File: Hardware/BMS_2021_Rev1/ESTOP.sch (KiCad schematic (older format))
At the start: 11 parts

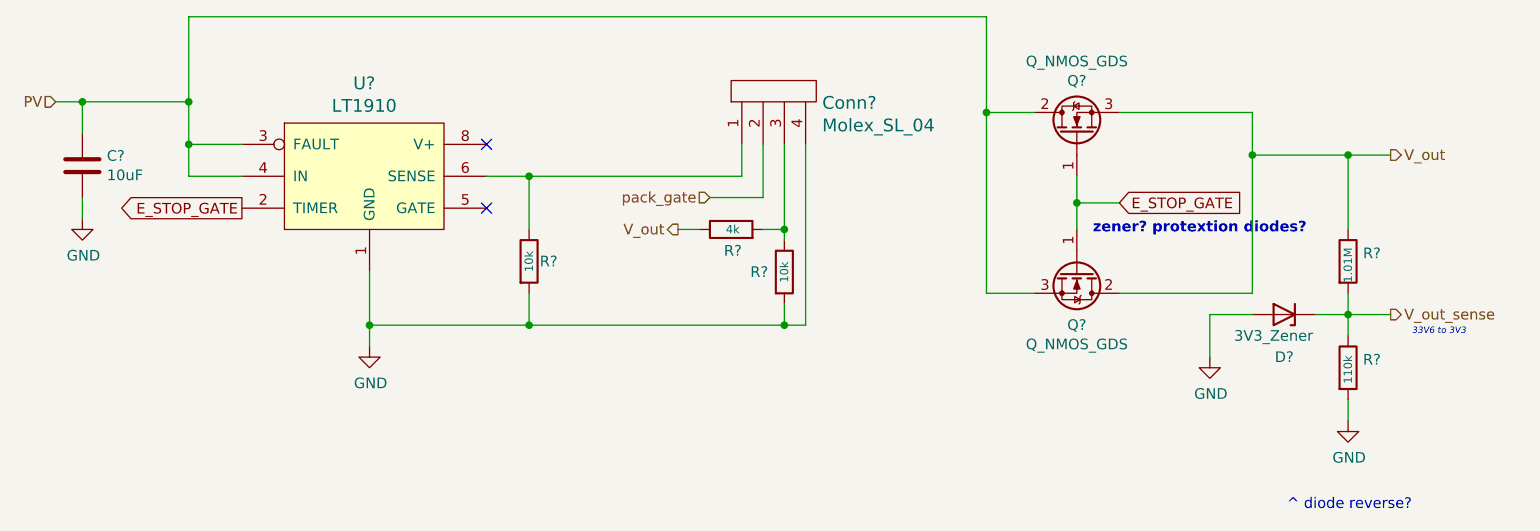
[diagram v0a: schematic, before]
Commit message: added libraries to docs folder
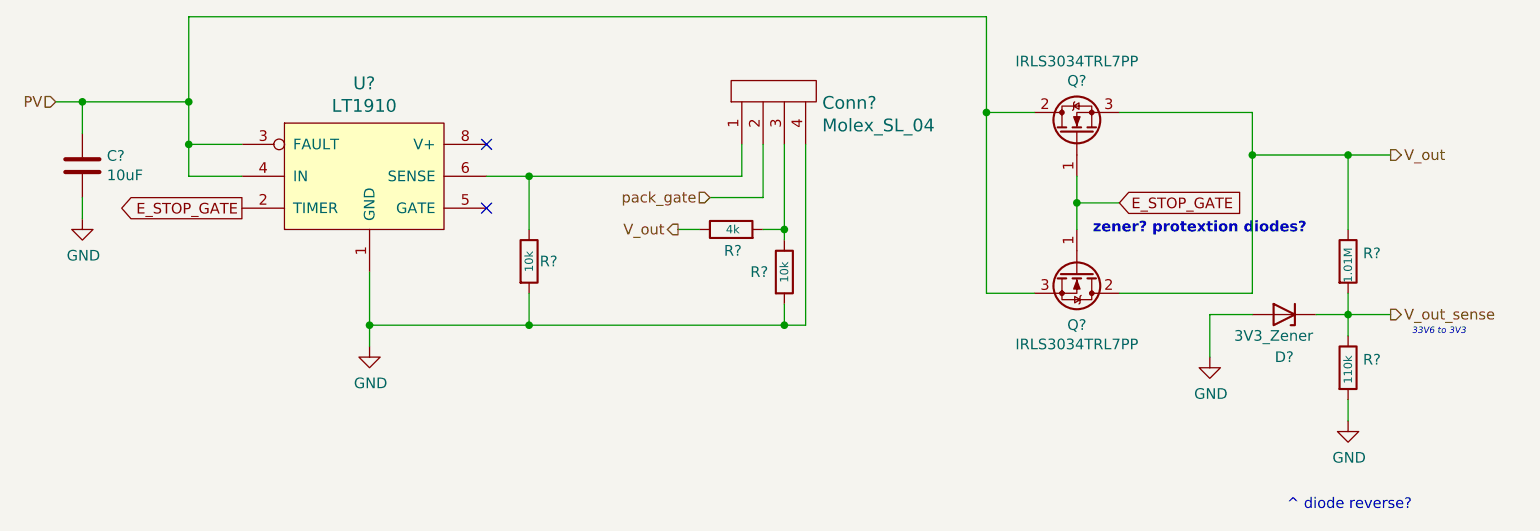
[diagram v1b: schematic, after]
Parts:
- Q? (x2): value Q_NMOS_GDS -> IRLS3034TRL7PP
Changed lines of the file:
@@
 P 7275 3300
 F 0 "Q?" V 7524 3300 50  0000 C CNN
-F 1 "Q_NMOS_GDS" V 7615 3300 50  0000 C CNN
+F 1 "IRLS3034TRL7PP" V 7615 3300 50  0000 C CNN
 F 2 "" H 7475 3400 50  0001 C CNN
-F 3 "~" H 7275 3300 50  0001 C CNN
+F 3 "https://www.digikey.com/en/products/detail/infineon-technologies/IRLS3034TRL7PP/2096641" H 7275 3300 50  0001 C CNN
 	1    7275 3300
 	0    1    1    0
@@
 P 7275 2650
 F 0 "Q?" V 7524 2650 50  0000 C CNN
-F 1 "Q_NMOS_GDS" V 7615 2650 50  0000 C CNN
+F 1 "IRLS3034TRL7PP" V 7615 2650 50  0000 C CNN
 F 2 "" H 7475 2750 50  0001 C CNN
-F 3 "~" H 7275 2650 50  0001 C CNN
+F 3 "https://www.digikey.com/en/products/detail/infineon-technologies/IRLS3034TRL7PP/2096641" H 7275 2650 50  0001 C CNN
 	1    7275 2650
 	0    -1   -1   0

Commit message: annotated sch.
some ICs got moved around- solve later
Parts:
- added D17: 3V3_Zener, symbol Device:D_Zener
- C11: renamed from C?; value 10uF -> 10u
- Q2, Q3: renamed from Q?; value IRLS3034TRL7PP -> IRLB3034PBF
- gave numbers to parts that had none: 8
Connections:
- net E_STOP_GATE: now also D17.1 (K)
- net GND: now also D17.2 (A)
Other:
- note removed: "^ diode reverse?"
- note removed: "zener? protextion diodes?"
- moved on the sheet: R40, R41
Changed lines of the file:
@@
 $EndDescr
 $Comp
-L MRDT_ICs:LT1910 U?
+L MRDT_ICs:LT1910 U7
 U 1 1 5F8B7AE9
 P 3550 3100
-F 0 "U?" H 3925 3787 60  0000 C CNN
+F 0 "U7" H 3925 3787 60  0000 C CNN
 F 1 "LT1910" H 3925 3681 60  0000 C CNN
 F 2 "" H 3550 3100 60  0001 C CNN
@@
 Connection ~ 3100 2700
 $Comp
-L Device:C C?
+L Device:C C11
 U 1 1 5F8B88FB
 P 2600 2800
-F 0 "C?" H 2715 2846 50  0000 L CNN
-F 1 "10uF" H 2715 2755 50  0000 L CNN
+F 0 "C11" H 2715 2846 50  0000 L CNN
+F 1 "10u" H 2715 2755 50  0000 L CNN
 F 2 "" H 2638 2650 50  0001 C CNN
 F 3 "~" H 2600 2800 50  0001 C CNN
@@
 	2600 2950 2600 3050
 $Comp
-L power:GND #PWR?
+L power:GND #PWR045
 U 1 1 5F8B8E29
 P 2600 3050
-F 0 "#PWR?" H 2600 2800 50  0001 C CNN
+F 0 "#PWR045" H 2600 2800 50  0001 C CNN
 F 1 "GND" H 2605 2877 50  0000 C CNN
 F 2 "" H 2600 3050 50  0001 C CNN
@@
 Connection ~ 4700 3550
 $Comp
-L Device:R R?
+L Device:R R37
 U 1 1 5F8B9A73
 P 4700 3250
-F 0 "R?" H 4750 3250 50  0000 L CNN
+F 0 "R37" H 4750 3250 50  0000 L CNN
 F 1 "10k" V 4700 3200 39  0000 L CNN
 F 2 "" V 4630 3250 50  0001 C CNN
@@
 	4700 3400 4700 3550
 $Comp
-L MRDT_Connectors:Molex_SL_04 Conn?
+L MRDT_Connectors:Molex_SL_04 Conn5
 U 1 1 5F8BA191
 P 6050 2500
-F 0 "Conn?" V 6045 2472 60  0000 R CNN
-F 1 "Molex_SL_04" V 5939 2472 60  0000 R CNN
+F 0 "Conn5" V 6100 3200 60  0000 R CNN
+F 1 "Molex_SL_04" V 6000 3475 60  0000 R CNN
 F 2 "" H 6050 2500 60  0001 C CNN
 F 3 "" H 6050 2500 60  0001 C CNN
@@
 	6000 3550 6000 2700
 $Comp
-L Device:R R?
+L Device:R R39
 U 1 1 5F8BD200
 P 5900 3300
-F 0 "R?" H 5740 3300 50  0000 L CNN
+F 0 "R39" H 5700 3300 50  0000 L CNN
 F 1 "10k" V 5900 3250 39  0000 L CNN
 F 2 "" V 5830 3300 50  0001 C CNN
@@
 	5800 2950 5550 2950
 $Comp
-L Device:R R?
+L Device:R R38
 U 1 1 5F8BD8B6
 P 5650 3100
-F 0 "R?" V 5550 3050 50  0000 L CNN
+F 0 "R38" V 5550 3050 50  0000 L CNN
 F 1 "4k" V 5650 3060 39  0000 L CNN
 F 2 "" V 5580 3100 50  0001 C CNN
@@
 Connection ~ 3950 3550
 $Comp
-L power:GND #PWR?
+L power:GND #PWR046
 U 1 1 5F8C9892
 P 3950 3650
-F 0 "#PWR?" H 3950 3400 50  0001 C CNN
+F 0 "#PWR046" H 3950 3400 50  0001 C CNN
 F 1 "GND" H 3955 3477 50  0000 C CNN
 F 2 "" H 3950 3650 50  0001 C CNN
@@
 $EndComp
 $Comp
-L Device:Q_NMOS_GDS Q?
+L Device:Q_NMOS_GDS Q3
 U 1 1 5F8F3525
 P 7275 3300
-F 0 "Q?" V 7524 3300 50  0000 C CNN
-F 1 "IRLS3034TRL7PP" V 7615 3300 50  0000 C CNN
+F 0 "Q3" V 7524 3300 50  0000 C CNN
+F 1 "IRLB3034PBF" V 7615 3300 50  0000 C CNN
 F 2 "" H 7475 3400 50  0001 C CNN
-F 3 "https://www.digikey.com/en/products/detail/infineon-technologies/IRLS3034TRL7PP/2096641" H 7275 3300 50  0001 C CNN
+F 3 "https://www.digikey.com/en/products/detail/infineon-technologies/IRLB3034PBF/2096638" H 7275 3300 50  0001 C CNN
 	1    7275 3300
 	0    1    1    0
 $EndComp
 $Comp
-L Device:Q_NMOS_GDS Q?
+L Device:Q_NMOS_GDS Q2
 U 1 1 5F8F352B
 P 7275 2650
-F 0 "Q?" V 7524 2650 50  0000 C CNN
-F 1 "IRLS3034TRL7PP" V 7615 2650 50  0000 C CNN
+F 0 "Q2" V 7524 2650 50  0000 C CNN
+F 1 "IRLB3034PBF" V 7615 2650 50  0000 C CNN
 F 2 "" H 7475 2750 50  0001 C CNN
-F 3 "https://www.digikey.com/en/products/detail/infineon-technologies/IRLS3034TRL7PP/2096641" H 7275 2650 50  0001 C CNN
+F 3 "https://www.digikey.com/en/products/detail/infineon-technologies/IRLB3034PBF/2096638" H 7275 2650 50  0001 C CNN
 	1    7275 2650
 	0    -1   -1   0
@@
 	7275 2975 7275 3100
 Wire Wire Line
-	7075 2550 6850 2550
-Wire Wire Line
-	6850 3400 7075 3400
-Wire Wire Line
 	7475 2550 8100 2550
 Wire Wire Line
@@
 Wire Wire Line
 	8100 3400 7475 3400
-Wire Wire Line
-	8100 2750 8550 2750
 Connection ~ 8100 2750
 Wire Wire Line
 	8100 2750 8100 3400
-Connection ~ 8550 2750
-Wire Wire Line
-	8550 2750 8750 2750
 Text HLabel 8750 2750 2    50   Output ~ 0
 V_out
@@
 L Device:R R?
 U 1 1 5F8F354D
-P 8550 3250
+P 8575 3250
 AR Path="/5F80136E/5F8F354D" Ref="R?"  Part="1"
 AR Path="/5F8CBCAE/5F8F354D" Ref="R?"  Part="1"
-AR Path="/5F801232/5F8F354D" Ref="R?"  Part="1"
-F 0 "R?" H 8620 3288 50  0000 L CNN
-F 1 "1.01M" V 8550 3150 39  0000 L CNN
-F 2 "" V 8480 3250 50  0001 C CNN
-F 3 "~" H 8550 3250 50  0001 C CNN
-	1    8550 3250
-	1    0    0    -1
-$EndComp
-$Comp
-L Device:R R?
+AR Path="/5F801232/5F8F354D" Ref="R40"  Part="1"
+F 0 "R40" H 8645 3288 50  0000 L CNN
+F 1 "1.01M" V 8575 3150 39  0000 L CNN
+F 2 "" V 8505 3250 50  0001 C CNN
+F 3 "~" H 8575 3250 50  0001 C CNN
+	1    8575 3250
+	1    0    0    -1
+$EndComp
+$Comp
+L Device:R R41
 U 1 1 5F8F3553
-P 8550 3750
-F 0 "R?" H 8620 3788 50  0000 L CNN
-F 1 "110k" V 8550 3675 39  0000 L CNN
-F 2 "" V 8480 3750 50  0001 C CNN
-F 3 "~" H 8550 3750 50  0001 C CNN
-	1    8550 3750
-	1    0    0    -1
-$EndComp
-Wire Wire Line
-	8550 3900 8550 4000
-Wire Wire Line
-	8550 3500 8750 3500
-Connection ~ 8550 3500
-Wire Wire Line
-	8550 3500 8550 3600
-$Comp
-L power:GND #PWR?
+P 8575 3750
+F 0 "R41" H 8645 3788 50  0000 L CNN
+F 1 "110k" V 8575 3675 39  0000 L CNN
+F 2 "" V 8505 3750 50  0001 C CNN
+F 3 "~" H 8575 3750 50  0001 C CNN
+	1    8575 3750
+	1    0    0    -1
+$EndComp
+Wire Wire Line
+	8575 3900 8575 4000
+Wire Wire Line
+	8575 3500 8775 3500
+Connection ~ 8575 3500
+Wire Wire Line
+	8575 3500 8575 3600
+$Comp
+L power:GND #PWR049
 U 1 1 5F8F355D
-P 8550 4000
-F 0 "#PWR?" H 8550 3750 50  0001 C CNN
-F 1 "GND" H 8555 3827 50  0000 C CNN
-F 2 "" H 8550 4000 50  0001 C CNN
-F 3 "" H 8550 4000 50  0001 C CNN
-	1    8550 4000
-	1    0    0    -1
-$EndComp
-$Comp
-L Device:D_Zener D?
+P 8575 4000
+F 0 "#PWR049" H 8575 3750 50  0001 C CNN
+F 1 "GND" H 8580 3827 50  0000 C CNN
+F 2 "" H 8575 4000 50  0001 C CNN
+F 3 "" H 8575 4000 50  0001 C CNN
+	1    8575 4000
+	1    0    0    -1
+$EndComp
+$Comp
+L Device:D_Zener D18
 U 1 1 5F8F3563
 P 8250 3500
-F 0 "D?" H 8250 3700 50  0000 C CNN
+F 0 "D18" H 8250 3700 50  0000 C CNN
 F 1 "3V3_Zener" H 8300 3600 50  0000 C CNN
 F 2 "" H 8250 3500 50  0001 C CNN
@@
 $EndComp
 Wire Wire Line
-	8400 3500 8550 3500
-Wire Wire Line
 	8100 3500 7900 3500
 Wire Wire Line
 	7900 3500 7900 3700
 $Comp
-L power:GND #PWR?
+L power:GND #PWR048
 U 1 1 5F8F356C
 P 7900 3700
-F 0 "#PWR?" H 7900 3450 50  0001 C CNN
+F 0 "#PWR048" H 7900 3450 50  0001 C CNN
 F 1 "GND" H 7905 3527 50  0000 C CNN
 F 2 "" H 7900 3700 50  0001 C CNN
@@
 $EndComp
 Wire Wire Line
-	8550 2750 8550 3100
-Wire Wire Line
-	8550 3400 8550 3500
-Text HLabel 8750 3500 2    50   Output ~ 0
+	8575 2750 8575 3100
+Wire Wire Line
+	8575 3400 8575 3500
+Text HLabel 8775 3500 2    50   Output ~ 0
 V_out_sense
 Text Notes 8850 3600 0    30   Italic 0
 33V6 to 3V3
-Text Notes 7350 3125 0    50   ~ 10
-zener? protextion diodes?
 Text GLabel 3350 3000 0    50   Output ~ 0
 E_STOP_GATE
@@
 E_STOP_GATE
 Wire Wire Line
-	6850 2550 6850 3400
+	6250 2550 6250 3400
 Wire Wire Line
 	2600 2500 3100 2500
@@
 	3100 2500 3100 2100
 Wire Wire Line
-	3100 2100 6850 2100
-Wire Wire Line
-	6850 2100 6850 2550
+	3100 2100 6250 2100
+Wire Wire Line
+	6250 2100 6250 2550
 Connection ~ 3100 2500
-Connection ~ 6850 2550
-Text Notes 8850 4425 2    50   ~ 0
-^ diode reverse?
+Connection ~ 6250 2550
+Connection ~ 8575 2750
+Wire Wire Line
+	8575 2750 8750 2750
+Wire Wire Line
+	8100 2750 8575 2750
+Wire Wire Line
+	8400 3500 8575 3500
+$Comp
+L Device:D_Zener D17
+U 1 1 5FA929CE
+P 6975 2975
+F 0 "D17" H 6975 3175 50  0000 C CNN
+F 1 "3V3_Zener" H 7025 3075 50  0000 C CNN
+F 2 "" H 6975 2975 50  0001 C CNN
+F 3 "~" H 6975 2975 50  0001 C CNN
+	1    6975 2975
+	-1   0    0    1
+$EndComp
+Wire Wire Line
+	6825 2975 6625 2975
+Wire Wire Line
+	6625 2975 6625 3175
+$Comp
+L power:GND #PWR047
+U 1 1 5FA929D6
+P 6625 3175
+F 0 "#PWR047" H 6625 2925 50  0001 C CNN
+F 1 "GND" H 6630 3002 50  0000 C CNN
+F 2 "" H 6625 3175 50  0001 C CNN
+F 3 "" H 6625 3175 50  0001 C CNN
+	1    6625 3175
+	1    0    0    -1
+$EndComp
+Wire Wire Line
+	7125 2975 7275 2975
+Wire Wire Line
+	6250 2550 7075 2550
+Wire Wire Line
+	6250 3400 7075 3400
 $EndSCHEMATC

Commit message: Began assigning footprints
Downloaded some footprint files from UltraLibrarian. Put in BMS_Hardware>Documentation> then copied files where they need to go
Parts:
- C11: footprint (none) -> Capacitor_THT:CP_Radial_D5.0mm_P2.50mm
- Conn5: footprint (none) -> MRDT_Connectors:MOLEX_SL_04_Vertical
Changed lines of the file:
@@
 F 0 "C11" H 2715 2846 50  0000 L CNN
 F 1 "10u" H 2715 2755 50  0000 L CNN
-F 2 "" H 2638 2650 50  0001 C CNN
-F 3 "~" H 2600 2800 50  0001 C CNN
+F 2 "Capacitor_THT:CP_Radial_D5.0mm_P2.50mm" H 2638 2650 50  0001 C CNN
+F 3 "https://www.digikey.com/en/products/detail/nichicon/UVR1H100MDD1TD/3438479" H 2600 2800 50  0001 C CNN
 	1    2600 2800
 	1    0    0    -1
@@
 F 0 "Conn5" V 6100 3200 60  0000 R CNN
 F 1 "Molex_SL_04" V 6000 3475 60  0000 R CNN
-F 2 "" H 6050 2500 60  0001 C CNN
+F 2 "MRDT_Connectors:MOLEX_SL_04_Vertical" H 6050 2500 60  0001 C CNN
 F 3 "" H 6050 2500 60  0001 C CNN
 	1    6050 2500

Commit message: more footprints added
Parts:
- R37, R38, R39, R40, R41: footprint (none) -> Resistor_SMD:R_0603_1608Metric_Pad1.05x0.95mm_HandSolder
- U7: footprint (none) -> MRDT_BMS2021:LT1910_SOIC-8-1EP_3.9x4.9mm_P1.27mm_EP2.41x3.3mm
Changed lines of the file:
@@
 F 0 "U7" H 3925 3787 60  0000 C CNN
 F 1 "LT1910" H 3925 3681 60  0000 C CNN
-F 2 "" H 3550 3100 60  0001 C CNN
+F 2 "MRDT_BMS2021:LT1910_SOIC-8-1EP_3.9x4.9mm_P1.27mm_EP2.41x3.3mm" H 3550 3100 60  0001 C CNN
 F 3 "" H 3550 3100 60  0001 C CNN
 	1    3550 3100
@@
 F 0 "R37" H 4750 3250 50  0000 L CNN
 F 1 "10k" V 4700 3200 39  0000 L CNN
-F 2 "" V 4630 3250 50  0001 C CNN
+F 2 "Resistor_SMD:R_0603_1608Metric_Pad1.05x0.95mm_HandSolder" V 4630 3250 50  0001 C CNN
 F 3 "~" H 4700 3250 50  0001 C CNN
 	1    4700 3250
@@
 F 0 "R39" H 5700 3300 50  0000 L CNN
 F 1 "10k" V 5900 3250 39  0000 L CNN
-F 2 "" V 5830 3300 50  0001 C CNN
+F 2 "Resistor_SMD:R_0603_1608Metric_Pad1.05x0.95mm_HandSolder" V 5830 3300 50  0001 C CNN
 F 3 "~" H 5900 3300 50  0001 C CNN
 	1    5900 3300
@@
 F 0 "R38" V 5550 3050 50  0000 L CNN
 F 1 "4k" V 5650 3060 39  0000 L CNN
-F 2 "" V 5580 3100 50  0001 C CNN
+F 2 "Resistor_SMD:R_0603_1608Metric_Pad1.05x0.95mm_HandSolder" V 5580 3100 50  0001 C CNN
 F 3 "~" H 5650 3100 50  0001 C CNN
 	1    5650 3100
@@
 F 0 "R40" H 8645 3288 50  0000 L CNN
 F 1 "1.01M" V 8575 3150 39  0000 L CNN
-F 2 "" V 8505 3250 50  0001 C CNN
+F 2 "Resistor_SMD:R_0603_1608Metric_Pad1.05x0.95mm_HandSolder" V 8505 3250 50  0001 C CNN
 F 3 "~" H 8575 3250 50  0001 C CNN
 	1    8575 3250
@@
 F 0 "R41" H 8645 3788 50  0000 L CNN
 F 1 "110k" V 8575 3675 39  0000 L CNN
-F 2 "" V 8505 3750 50  0001 C CNN
+F 2 "Resistor_SMD:R_0603_1608Metric_Pad1.05x0.95mm_HandSolder" V 8505 3750 50  0001 C CNN
 F 3 "~" H 8575 3750 50  0001 C CNN
 	1    8575 3750

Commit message: more footprints added
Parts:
- Q2, Q3: footprint (none) -> MRDT_BMS2021:IRLB3034PBF
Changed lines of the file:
@@
 F 0 "Q3" V 7524 3300 50  0000 C CNN
 F 1 "IRLB3034PBF" V 7615 3300 50  0000 C CNN
-F 2 "" H 7475 3400 50  0001 C CNN
+F 2 "MRDT_BMS2021:IRLB3034PBF" H 7475 3400 50  0001 C CNN
 F 3 "https://www.digikey.com/en/products/detail/infineon-technologies/IRLB3034PBF/2096638" H 7275 3300 50  0001 C CNN
 	1    7275 3300
@@
 F 0 "Q2" V 7524 2650 50  0000 C CNN
 F 1 "IRLB3034PBF" V 7615 2650 50  0000 C CNN
-F 2 "" H 7475 2750 50  0001 C CNN
+F 2 "MRDT_BMS2021:IRLB3034PBF" H 7475 2750 50  0001 C CNN
 F 3 "https://www.digikey.com/en/products/detail/infineon-technologies/IRLB3034PBF/2096638" H 7275 2650 50  0001 C CNN
 	1    7275 2650

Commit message: Layout generated v1
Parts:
- D17, D18: footprint (none) -> Diode_SMD:D_0603_1608Metric_Pad1.05x0.95mm_HandSolder
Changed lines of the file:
@@
 F 0 "D18" H 8250 3700 50  0000 C CNN
 F 1 "3V3_Zener" H 8300 3600 50  0000 C CNN
-F 2 "" H 8250 3500 50  0001 C CNN
+F 2 "Diode_SMD:D_0603_1608Metric_Pad1.05x0.95mm_HandSolder" H 8250 3500 50  0001 C CNN
 F 3 "~" H 8250 3500 50  0001 C CNN
 	1    8250 3500
@@
 F 0 "D17" H 6975 3175 50  0000 C CNN
 F 1 "3V3_Zener" H 7025 3075 50  0000 C CNN
-F 2 "" H 6975 2975 50  0001 C CNN
+F 2 "Diode_SMD:D_0603_1608Metric_Pad1.05x0.95mm_HandSolder" H 6975 2975 50  0001 C CNN
 F 3 "~" H 6975 2975 50  0001 C CNN
 	1    6975 2975

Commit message: Q2,3 footprint updated, via stitched V_in, TIVA moved
-need to update schematic symbols Q2,3
-double check TIVA orientation
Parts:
- Q2, Q3: footprint MRDT_BMS2021:IRLB3034PBF -> MRDT_Actives:IRLS3034_TO-263-7_P
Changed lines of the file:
@@
 F 0 "Q3" V 7524 3300 50  0000 C CNN
 F 1 "IRLB3034PBF" V 7615 3300 50  0000 C CNN
-F 2 "MRDT_BMS2021:IRLB3034PBF" H 7475 3400 50  0001 C CNN
+F 2 "MRDT_Actives:IRLS3034_TO-263-7_P" H 7475 3400 50  0001 C CNN
 F 3 "https://www.digikey.com/en/products/detail/infineon-technologies/IRLB3034PBF/2096638" H 7275 3300 50  0001 C CNN
 	1    7275 3300
@@
 F 0 "Q2" V 7524 2650 50  0000 C CNN
 F 1 "IRLB3034PBF" V 7615 2650 50  0000 C CNN
-F 2 "MRDT_BMS2021:IRLB3034PBF" H 7475 2750 50  0001 C CNN
+F 2 "MRDT_Actives:IRLS3034_TO-263-7_P" H 7475 2750 50  0001 C CNN
 F 3 "https://www.digikey.com/en/products/detail/infineon-technologies/IRLB3034PBF/2096638" H 7275 2650 50  0001 C CNN
 	1    7275 2650

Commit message: started updating footprint/symbol lib for new mosfet
cant' find where the file went, will investigate tomorrow
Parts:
- Q2, Q3: footprint MRDT_Actives:IRLS3034_TO-263-7_P -> MRDT_BMS2021:IRFS7530TRL7PP
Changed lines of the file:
@@
 F 0 "Q3" V 7524 3300 50  0000 C CNN
 F 1 "IRLB3034PBF" V 7615 3300 50  0000 C CNN
-F 2 "MRDT_Actives:IRLS3034_TO-263-7_P" H 7475 3400 50  0001 C CNN
+F 2 "MRDT_BMS2021:IRFS7530TRL7PP" H 7475 3400 50  0001 C CNN
 F 3 "https://www.digikey.com/en/products/detail/infineon-technologies/IRLB3034PBF/2096638" H 7275 3300 50  0001 C CNN
 	1    7275 3300
@@
 F 0 "Q2" V 7524 2650 50  0000 C CNN
 F 1 "IRLB3034PBF" V 7615 2650 50  0000 C CNN
-F 2 "MRDT_Actives:IRLS3034_TO-263-7_P" H 7475 2750 50  0001 C CNN
+F 2 "MRDT_BMS2021:IRFS7530TRL7PP" H 7475 2750 50  0001 C CNN
 F 3 "https://www.digikey.com/en/products/detail/infineon-technologies/IRLB3034PBF/2096638" H 7275 2650 50  0001 C CNN
 	1    7275 2650
